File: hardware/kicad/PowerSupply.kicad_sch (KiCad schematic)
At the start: 3 parts

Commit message: Phase A3: hierarchical V1 schematic generated from pstxnet.dat, ERC clean, netlist == pstxnet
gen_symbols.py (R1240N001x, TCAN1042H-Q1, CMS06 diode, VIN_RAW power symbol per current datasheets),
kicad_sym.py (flattened embedding of KiCad 9 library symbols), gen_sch.py (7 sub-sheets mirroring the OrCAD
blocks, labels/hierarchical pins/power symbols, deterministic symbol paths shared with the PCB via v1_design.py),
check_netlist.py (schematic and board nets == pstxnet.dat, refs and footprint paths match).
ERC 0 violations with --severity-all. Allegro refdes without a trailing digit get a '1' suffix (KiCad annotation
rule); original kept in the Allegro_RefDes property.

Co-Authored-By: Claude Fable 5.1 <noreply@anthropic.com>
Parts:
- removed _TEMPLATE_C: C_TEMPLATE, symbol Device:C
- removed _TEMPLATE_D: LED_TEMPLATE, symbol Device:LED
- removed _TEMPLATE_R: R_TEMPLATE, symbol Device:R
- added C12: 1uF, LoRa_Boat_Controller:CAP_CL10_SAM-M, symbol Device:C
- added C14: 470pF, LoRa_Boat_Controller:CAP_0603G_AVX-M, symbol Device:C
- added CIN1: 10uF, LoRa_Boat_Controller:CAP_NTS_55_2P8T_NIP, symbol Device:C
- added COUT1: 10uF, LoRa_Boat_Controller:G-31_MUR-M, symbol Device:C
- added D21: CMS06(TE12L,Q,M), LoRa_Boat_Controller:M-FLAT_TOS-L, symbol LoRa_Boat_Controller:CMS06_Schottky
- added GND1: Battery-, LoRa_Boat_Controller:amv_con1, symbol Connector_Generic:Conn_01x01
- added L1: 4.7uH, LoRa_Boat_Controller:IND_7045_TDK, symbol Device:L
- added R1: 15k, LoRa_Boat_Controller:RC0402N_PAN-M, symbol Device:R
- added R2: 4.7k, LoRa_Boat_Controller:RC0603N_YAG-M, symbol Device:R
- added R3: 51, LoRa_Boat_Controller:RC0402N_YAG-M, symbol Device:R
- added R4: 5.1k, LoRa_Boat_Controller:RC0402N_PAN-M, symbol Device:R
- added R5: 30k, LoRa_Boat_Controller:RES_R0805_ROM-M, symbol Device:R
- added R6: 10k, LoRa_Boat_Controller:RES_1005_SAM-M, symbol Device:R
- added TP4, TP5: TP, LoRa_Boat_Controller:amv_test_point, symbol Connector:TestPoint
- added U6: R1240N001B-TR-FE, LoRa_Boat_Controller:SOT-23-6W_PE-SOT23-6W-0512_NMD, symbol LoRa_Boat_Controller:R1240N001x
- added VIN1: Battery+, LoRa_Boat_Controller:amv_con1, symbol Connector_Generic:Conn_01x01
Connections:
- new net +3V3: C14.1, COUT1.2, L1.1, R1.1, TP4.1
- new net ADC_VBAT: R5.2, R6.2
- new net BST: R3.2, U6.4 (BST)
- new net BST_RC: C12.2, R3.1
- new net EN: R4.2, U6.1 (CE)
- new net FB_DIV: C14.2, R1.2, R2.1, U6.6 (VFB)
- new net GND: CIN1.1, COUT1.1, D21.1 (A), GND1.1 (Pin_1), R2.2, R6.1, TP5.1, U6.5 (GND)
- new net SW_NODE: C12.1, D21.2 (K), L1.2, U6.3 (LX)
- new net VIN_RAW: CIN1.2, R4.1, R5.1, U6.2 (VIN), VIN1.1 (Pin_1)
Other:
- note added: "Allegro net names: +3V3<-3.3V, ADC_VBAT<-ADC, BST<-N17942, BST_RC<-N061071, EN<-N148600, FB_DIV<-N17576, GND<-0, SW_NODE<-N18028, VIN_RAW<-N088060"
- note added: "PWR_FLAG: VIN_RAW comes from the battery solder pad, +3V3 from L1 - neither is a power output pin"
- note added: "PowerSupply: OrCAD blocks: Power Supply / POWER BLOCK (battery pads, R1240N buck, D21 catch diode, VBAT divider, TP4/TP5)"
- company: (none) -> University of Arkansas EECS
- title: (none) -> LoRa Autonomous Boat Controller V1 - PowerSupply

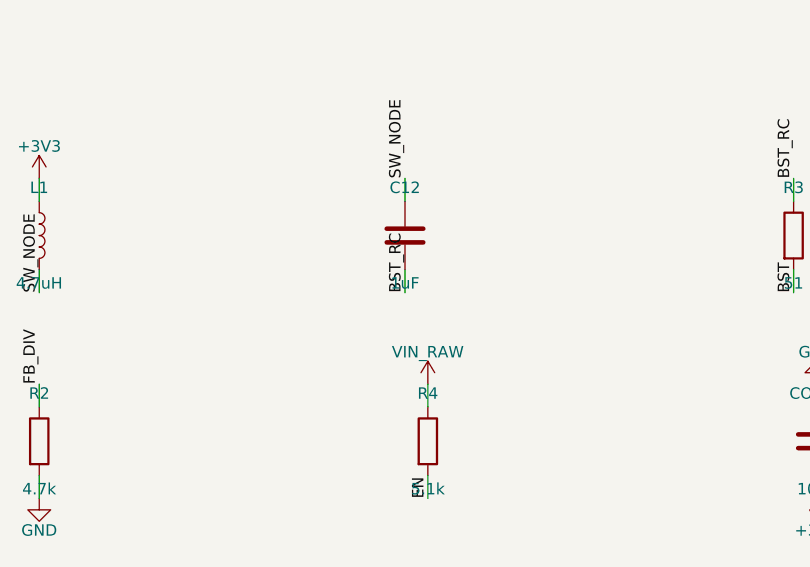
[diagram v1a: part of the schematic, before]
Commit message: Phase A3 close: CANH/CANL net names corrected, BOM with MPNs, DSN-v2 comparison, schematic exports
- gen_pcb.py: N04855 is CANL (U5 pin 6) and N24691 is CANH (U5 pin 7) per pstxnet.dat + TI SLLSES9D; the
  old NETLIST.md had them reversed (Codex review finding R03).
- gen_bom.py: docs/BOM.csv regenerated from the schematic with MPN/manufacturer/description/confidence/price
  columns (research in docs/research/BOM_MPN_RESEARCH.md, prices 2026-09-16).
- a0_xor_dsn.py: DSN v2 copper vs v5 films = 54 % / 63 % mismatch, 0 of 20 vias coincide, 0 of 45 parts unmoved;
  the DSN wiring is unusable for v5 (documented in docs/A0_PROVENANCE.md).
- Schematic PDF and per-sheet SVG exports in docs/img.
Gates: DRC 0 errors / 0 unconnected, ERC 0 violations, netlist check PASS, XOR F.Cu 0.87 % B.Cu 0.23 %.

Co-Authored-By: Claude Fable 5.1 <noreply@anthropic.com>
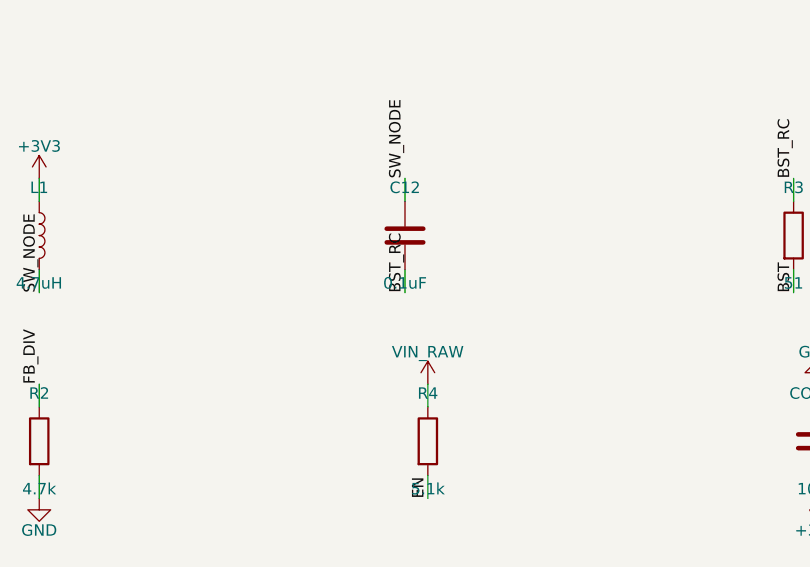
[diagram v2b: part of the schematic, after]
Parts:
- C12: value 1uF -> 0.1uF; MPN (none) -> CL10B104KB8NNNC; Manufacturer (none) -> Samsung Electro-Mechanics
- C14: MPN (none) -> 06035A471JAT2A; Manufacturer (none) -> Kyocera AVX
- CIN1: MPN (none) -> KTS500B106M55N0T00; Manufacturer (none) -> Nippon Chemi-Con
- COUT1: MPN (none) -> GRM31CR71E106KA12L; Manufacturer (none) -> Murata
- D21: MPN (none) -> CMS06(TE12L,Q,M); Manufacturer (none) -> Toshiba
- L1: MPN (none) -> SLF7045T-4R7M2R0-PF; Manufacturer (none) -> TDK
- R1: MPN (none) -> ERJ-2RKF1502X; Manufacturer (none) -> Panasonic
- R2: MPN (none) -> RC0603FR-074K7L; Manufacturer (none) -> Yageo
- R3: MPN (none) -> RC0402FR-0751RL; Manufacturer (none) -> Yageo
- R4: MPN (none) -> ERJ-2RKF5101X; Manufacturer (none) -> Panasonic
- R5: MPN (none) -> RC0805FR-0730KL; Manufacturer (none) -> Yageo
- R6: MPN (none) -> RC1005F103CS; Manufacturer (none) -> Samsung Electro-Mechanics
- U6: MPN (none) -> R1240N001B-TR-FE; Manufacturer (none) -> Nisshinbo Micro Devices (ex-Ricoh)
